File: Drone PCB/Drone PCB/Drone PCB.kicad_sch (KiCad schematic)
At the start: 36 parts, among them J3 Conn_01x02_Socket, J3 Conn_01x06_Socket, J4 Conn_01x06_Pin, Q1 SI2302, Q2 SI2302, Q3 SI2302, Q4 SI2302, SW1 SW_Push, SW1 SW_SPDT, U1 AMS1117-3.3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

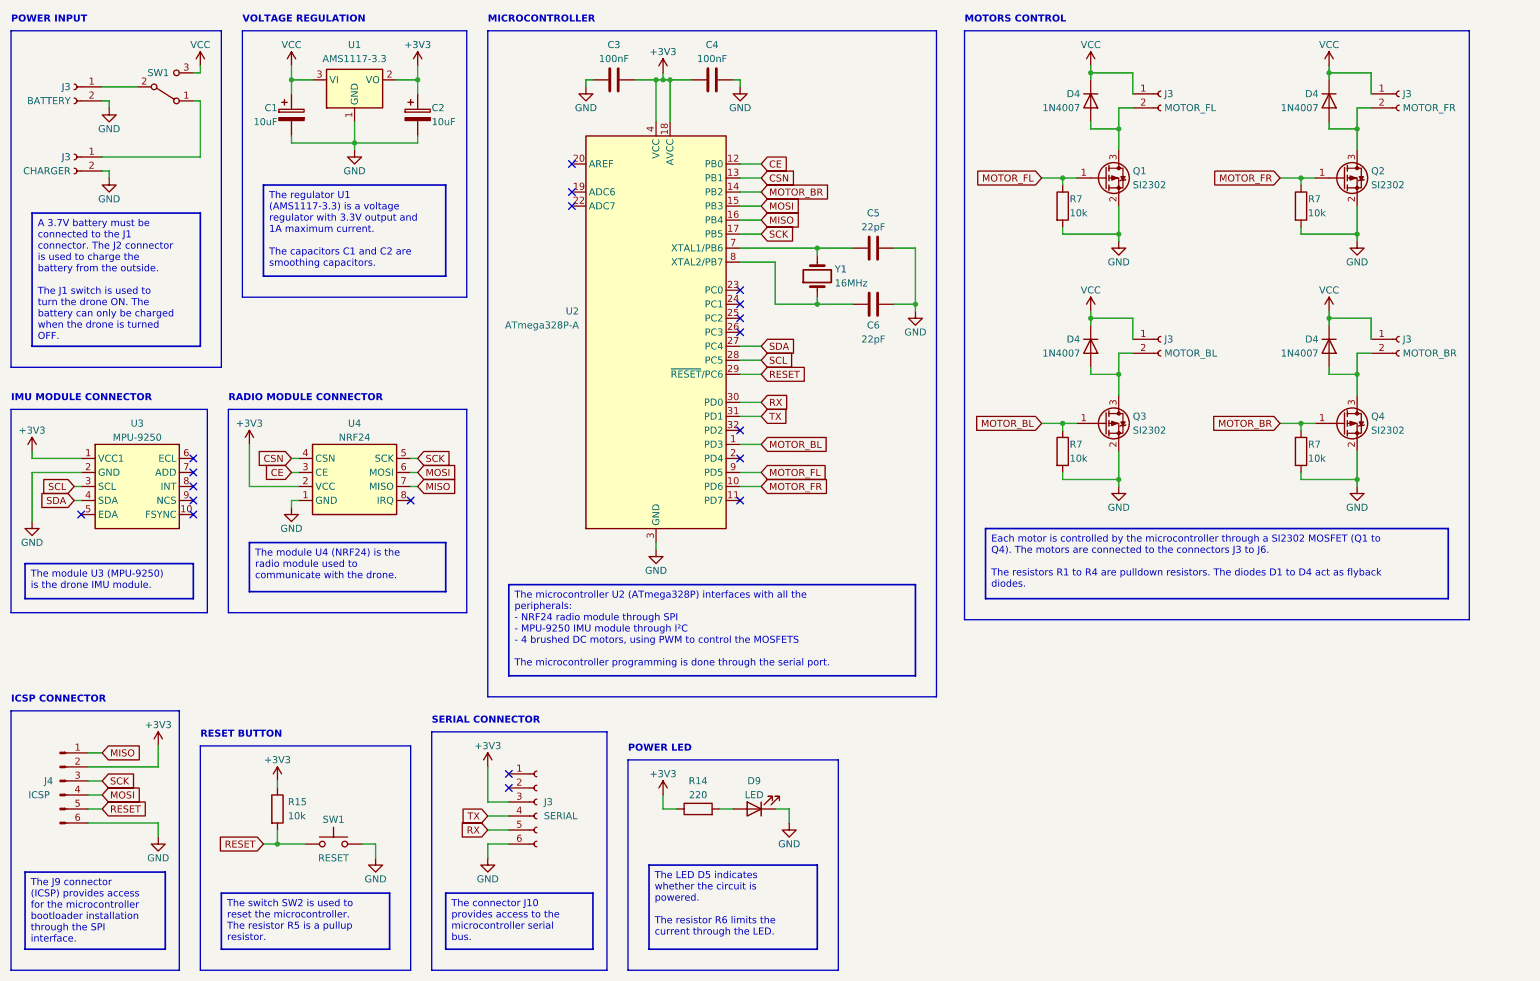
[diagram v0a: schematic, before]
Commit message: PCB layout improved
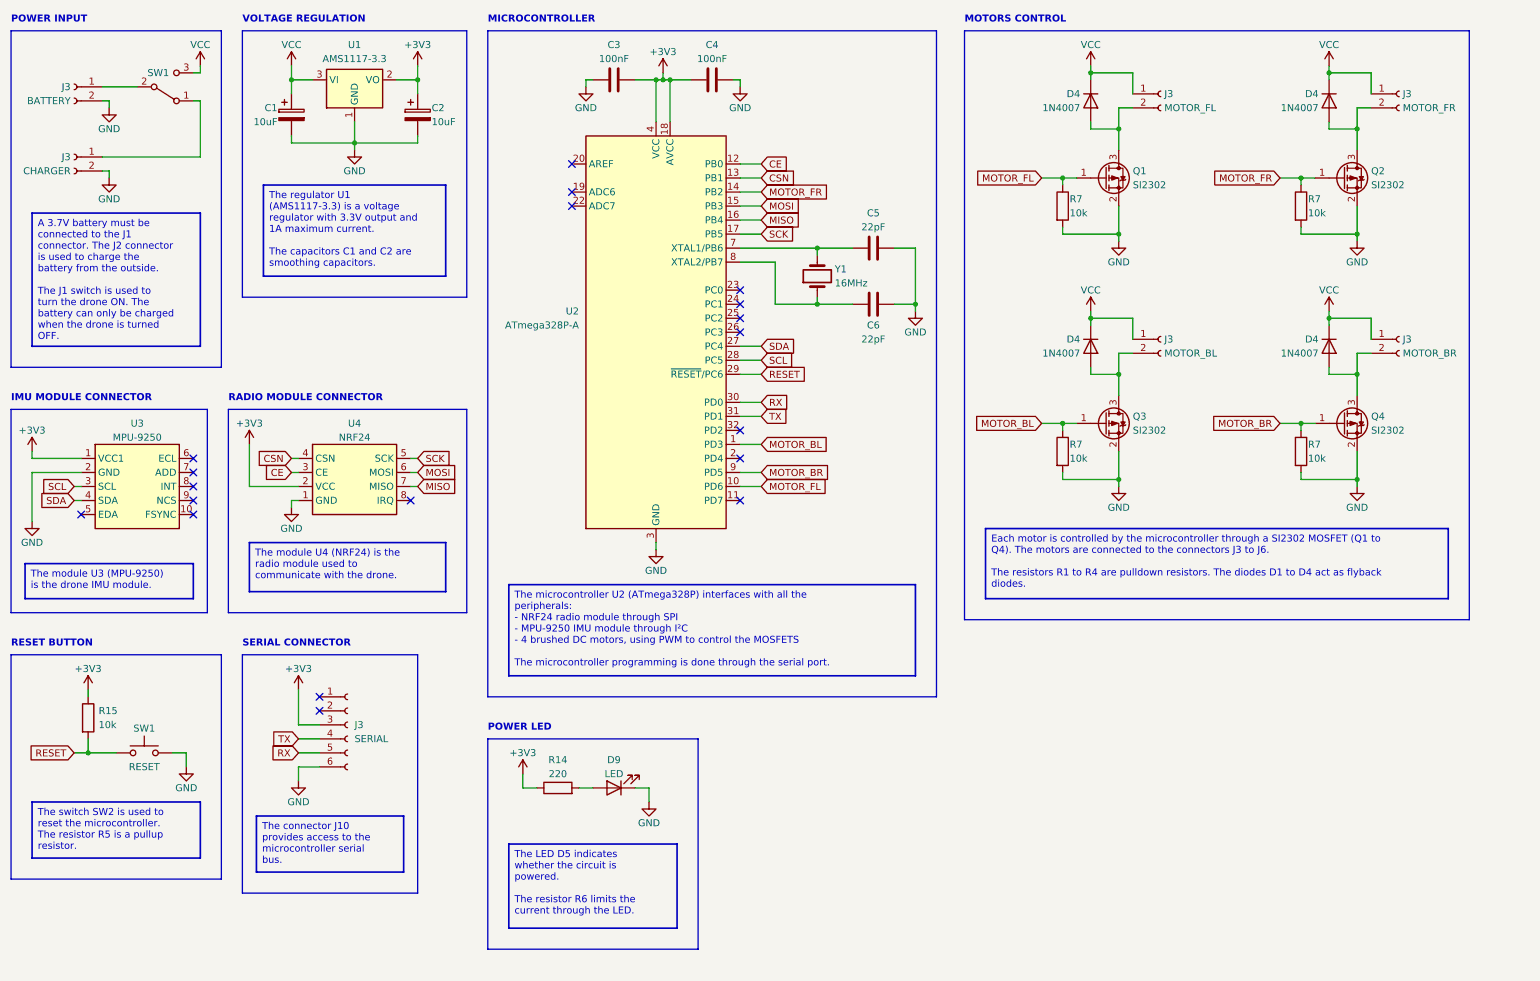
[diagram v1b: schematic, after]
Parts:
- removed J4: Conn_01x06_Pin, Connector_PinSocket_2.54mm:PinSocket_2x03_P2.54mm_Vertical, symbol Connector:Conn_01x06_Pin
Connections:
- net MOTOR_BR: now also U2.9 (PD5); no longer U2.14 (PB2)
- net MOTOR_FL: now also U2.10 (PD6); no longer U2.9 (PD5)
- net MOTOR_FR: now also U2.14 (PB2); no longer U2.10 (PD6)
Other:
- note removed: "ICSP CONNECTOR"
- moved on the sheet: D9, J3, R14, R15, SW1
